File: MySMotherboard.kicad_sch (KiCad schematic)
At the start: 45 parts, among them IC1 TS5205, IC2 25SN, IC3 ATSHA204A, IC4 MCP1640CT-I/CHY, IC5 ATMEGA328P-AU, J1 SJ2W, J2 SJ, Q1 PMOSSOT23, Q2 FA-128, X1 JST-PH2, X2 MA10-2

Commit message: refactor schematic to use native KiCad symbols and footprints
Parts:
- removed ANT0: WIREPAD2,15/1,0, MySMotherboard:2,15_1,0, symbol MySMotherboard-eagle-import:WIREPAD2,15/1,0
- removed BTN0, RST0: DTSM-3, MySMotherboard:DTSM-3, symbol MySMotherboard-eagle-import:DTSM-3
- removed C1, C13, C14, C3: 10u, MySMotherboard:C0603K, symbol MySMotherboard-eagle-import:C-EUC0603K
- removed C10, C4, C5, C6, C7: 100n, MySMotherboard:C0402, symbol MySMotherboard-eagle-import:C-EUC0402
- removed C12: 10n, MySMotherboard:C0402, symbol MySMotherboard-eagle-import:C-EUC0402
- removed C2: 4.7u, MySMotherboard:C0603K, symbol MySMotherboard-eagle-import:C-EUC0603K
- removed C8, C9: 22p, MySMotherboard:0402-CAP, symbol MySMotherboard-eagle-import:CAP0402-CAP
- removed CR123A0: BAT_PACKCR123A, MySMotherboard:BH123A, symbol MySMotherboard-eagle-import:BAT_PACKCR123A
- removed CR2032: WA-BCPH_SMT_79527141, MySMotherboard:79527141, symbol MySMotherboard-eagle-import:WA-BCPH_SMT_79527141
- removed D1: LEDCHIP-LED0805, MySMotherboard:CHIP-LED0805, symbol MySMotherboard-eagle-import:LEDCHIP-LED0805
- removed IC1: TS5205, MySMotherboard:SOT25, symbol MySMotherboard-eagle-import:TS5205
- removed IC2: 25SN, MySMotherboard:SO-08, symbol MySMotherboard-eagle-import:25SN
- removed IC3: ATSHA204A, MySMotherboard:SOT23, symbol MySMotherboard-eagle-import:ATSHA204A
- removed IC4: MCP1640CT-I/CHY, MySMotherboard:SOT95P270X145-6N, symbol MySMotherboard-eagle-import:MCP1640CT-I/CHY
- removed IC5: ATMEGA328P-AU, MySMotherboard:QFP80P900X900X120-32N, symbol MySMotherboard-eagle-import:ATMEGA328P-AU
- removed J1: SJ2W, MySMotherboard:SJ_2, symbol MySMotherboard-eagle-import:SJ2W
- removed J2: SJ, MySMotherboard:SJ, symbol MySMotherboard-eagle-import:SJ
- removed L1: 4.7u, MySMotherboard:L3225P, symbol MySMotherboard-eagle-import:L-EUL3225P
- removed NRF24L01: WIRELESS-NRF24L01, MySMotherboard:WIRELESS-NRF24L01, symbol MySMotherboard-eagle-import:WIRELESS-NRF24L01
- removed Q1: PMOSSOT23, MySMotherboard:SOT-23, symbol MySMotherboard-eagle-import:PMOSSOT23
- removed Q2: FA-128, MySMotherboard:FA-128, symbol MySMotherboard-eagle-import:FA-128
- removed R1, R11, R2, R3, R7: 1M, MySMotherboard:R0603, symbol MySMotherboard-eagle-import:R-US_R0603
- removed R10, R9: 10k, MySMotherboard:R0603, symbol MySMotherboard-eagle-import:R-US_R0603
- removed R12: 0, MySMotherboard:0603-RES, symbol MySMotherboard-eagle-import:RESISTOR0603-RES
- removed R4: 620k, MySMotherboard:R0603, symbol MySMotherboard-eagle-import:R-US_R0603
- removed R5: 1M, MySMotherboard:0603-RES, symbol MySMotherboard-eagle-import:RESISTOR0603-RES
- removed R6: 100k, MySMotherboard:0603-RES, symbol MySMotherboard-eagle-import:RESISTOR0603-RES
- removed R8: 1k, MySMotherboard:R0603, symbol MySMotherboard-eagle-import:R-US_R0603
- removed RFM69W0: RFM69HW, MySMotherboard:RFM, symbol MySMotherboard-eagle-import:RFM69HW
- removed X1: JST-PH2, MySMotherboard:JST-PH2, symbol MySMotherboard-eagle-import:JST-PH2
- removed X2: MA10-2, MySMotherboard:MA10-2, symbol MySMotherboard-eagle-import:MA10-2
- added BT1: CR2032, Battery:BatteryHolder_Keystone_1060_1x2032, symbol Device:Battery_Cell
- added BT2: CR123A, MySMotherboard:BH123A, symbol Device:Battery_Cell
- added C1, C13, C2, C3: 10u, Capacitor_SMD:C_0603_1608Metric, symbol Device:C
- added C10, C12, C4, C5, C7: 100n, Capacitor_SMD:C_0402_1005Metric, symbol Device:C
- added C14: 10u/16V, Capacitor_SMD:C_0603_1608Metric, symbol Device:C
- added C8, C9: 22p, Capacitor_SMD:C_0402_1005Metric, symbol Device:C
- added D1: LED, LED_SMD:LED_0805_2012Metric_Pad1.15x1.40mm_HandSolder, symbol Device:LED
- added JP1, JP3: ~, Jumper:SolderJumper-2_P1.3mm_Open_RoundedPad1.0x1.5mm, symbol Jumper:Jumper_2_Open
- added JP2: ~, Jumper:SolderJumper-3_P1.3mm_Open_RoundedPad1.0x1.5mm, symbol Jumper:Jumper_3_Open
- added L1: 4.7u, Inductor_SMD:L_1210_3225Metric_Pad1.42x2.65mm_HandSolder, symbol Device:L
- added NRF24L1: WIRELESS-NRF24L01, MySMotherboard:WIRELESS-NRF24L01, symbol MySMotherboard:WIRELESS-NRF24L01
- added Q1: ~, Package_TO_SOT_SMD:SOT-23, symbol Device:Q_PMOS_GSD
- added R1, R11, R2, R3, R5, R7: 1M, Resistor_SMD:R_0603_1608Metric, symbol Device:R
- added R10, R9: 10k, Resistor_SMD:R_0603_1608Metric, symbol Device:R
- added R4: 620k, Resistor_SMD:R_0603_1608Metric, symbol Device:R
- added R6: 100k, Resistor_SMD:R_0603_1608Metric, symbol Device:R
- added R8: 1k, Resistor_SMD:R_0603_1608Metric, symbol Device:R
- added SW1: RST, Button_Switch_SMD:SW_SPST_EVQPE1, symbol Switch:SW_Push
- added SW2: BTN, Button_Switch_SMD:SW_SPST_EVQPE1, symbol Switch:SW_Push
- added U1: MCP1640Cx-xCHY, Package_TO_SOT_SMD:SOT-23-6, symbol Regulator_Switching:MCP1640Cx-xCHY
- added U2: APE8865Y5-30-HF-3, Package_TO_SOT_SMD:SOT-23-5, symbol Regulator_Linear:APE8865Y5-30-HF-3
- added U3: ATmega328PB-A, Package_QFP:TQFP-32_7x7mm_P0.8mm, symbol MCU_Microchip_ATmega:ATmega328PB-A
- added U4: AT25xxx, Package_SO:SOIC-8_3.9x4.9mm_P1.27mm, symbol Memory_EEPROM:AT25xxx
- added U5: RFM69HW, RF_Module:HOPERF_RFM69HW, symbol RF_Module:RFM69HW
- added U6: ATSHA204A, Package_TO_SOT_SMD:SOT-23, symbol MySMotherboard:ATSHA204A
- added X1: ~, Connector_JST:JST_PH_B2B-PH-K_1x02_P2.00mm_Vertical, symbol Connector:Conn_01x02_Pin
- added X2: MySX 2.5, Connector_PinHeader_2.54mm:PinHeader_2x10_P2.54mm_Vertical, symbol Connector_Generic:Conn_02x10_Odd_Even
- added X3: ANT, Connector_PinHeader_2.54mm:PinHeader_1x01_P2.54mm_Vertical, symbol Connector:Conn_01x01_Pin
- added Y1: 16M, Crystal:Crystal_SMD_2520-4Pin_2.5x2.0mm, symbol Device:Crystal_GND24
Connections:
- net A0: now also U3.23 (PC0), X2.8 (Pin_8)
- net A1: now also R8.2, U3.24 (PC1), X2.20 (Pin_20)
- net A2: now also R11.1, U1.3 (EN), U3.25 (PC2)
- net A3: now also U3.26 (PC3), U6.1 (SDA)
- net A4: now also R10.2, U3.27 (PC4), X2.14 (Pin_14)
- net A5: now also R9.2, U3.28 (PC5), X2.13 (Pin_13)
- net A7: now also C4.1, R5.2, R6.1, U3.22 (PE3)
- net D10: now also NRF24L1.4 (CSN), R1.2, U3.14 (PB2), U5.15 (NSS)
- net D2: now also JP3.1 (A), U3.32 (PD2), X2.9 (Pin_9)
- net D3: now also SW2.1, U3.1 (PD3), X2.10 (Pin_10)
- net D4: now also U3.2 (PD4), X2.15 (Pin_15)
- net D5: now also U3.9 (PD5), X2.11 (Pin_11)
- net D6: now also U3.10 (PD6), X2.12 (Pin_12)
- net D7: now also U3.11 (PD7), X2.16 (Pin_16)
- net D8: now also R2.2, U3.12 (PB0), U4.1 (~{CS})
- net D9: now also NRF24L1.3 (CE), U3.13 (PB1)
- net GND: now also BT1.2 (-), BT2.2 (-), C1.1, C10.2, C12.2, C13.2, C14.2, C2.2, C3.2, C4.2, C5.2, C7.2, C8.1, C9.2, NRF24L1.1 (GND), Q1.1 (G), R11.2, R4.2, R6.2, SW1.2, SW2.2, U1.2 (GND), U2.2 (GND), U3.21 (GND), U3.5 (GND), U4.4 (GND), U5.11 (GND), U5.9 (GND), U6.3 (GND), X1.2 (Pin_2), X2.4 (Pin_4), Y1.2, Y1.4
- net MISO: now also NRF24L1.7 (MISO), U3.16 (PB4), U4.2 (MISO), U5.13 (MISO), X2.18 (Pin_18)
- net MOSI: now also NRF24L1.6 (MOSI), U3.15 (PB3), U4.5 (MOSI), U5.14 (MOSI), X2.17 (Pin_17)
- net RST: now also R7.2, SW1.1, U3.29 (~{RESET}/PC6), X2.7 (Pin_7)
- net RX: now also U3.30 (PD0), X2.6 (Pin_6)
- net SCK: now also NRF24L1.5 (SCK), U3.17 (PB5), U4.6 (SCK), U5.12 (SCK), X2.19 (Pin_19)
- net TX: now also U3.31 (PD1), X2.5 (Pin_5)
- net VBAT: now also C14.1, C2.1, L1.1, Q1.2 (S), R5.1, U1.6 (V_{IN}), U2.1 (VIN), U2.3 (~{SHDN})
- net VBOOST: now also C3.1, JP2.1 (A), R3.1, U1.5 (V_{OUT})
- net VCC: now also C1.2, C5.1, C7.1, D1.2 (A), JP2.2 (C), NRF24L1.2 (VCC), R1.1, R10.1, R2.1, R7.1, R9.1, U3.18 (AVCC), U3.4 (VCC), U4.3 (~{WP}), U4.7 (~{HOLD}), U4.8 (VCC), U5.8 (3.3V), U6.2 (VCC), X2.2 (Pin_2), X2.3 (Pin_3)
- net VRAW: now also JP1.1 (A), X2.1 (Pin_1)
- net VREG: now also C13.1, JP2.3 (B), U2.5 (VOUT)
- new net: JP3.2 (B), NRF24L1.8 (IRQ), U5.2 (DIO0)
- new net: R3.2, R4.1, U1.4 (V_{FB})
- new net: D1.1 (K), R8.1
- new net: C12.1, U2.4 (BYP)
- new net: C8.2, U3.8 (XTAL2/PB7), Y1.1
- new net: C9.1, U3.7 (XTAL1/PB6), Y1.3
- new net: U5.10 (ANA), X3.1 (Pin_1)
- new net: C10.1, U3.20 (AREF)
- new net SW_L: L1.2, U1.1 (SW)
- new net VIN: BT1.1 (+), BT2.1 (+), JP1.2 (B), Q1.3 (D), X1.1 (Pin_1)
- no-connect marks 0 -> 9
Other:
- note added: "Crypto"
- note added: "DC/DC boost comverter"
- note added: "LDO Regulator"
- note added: "MCU"
- note added: "MySX Connector"
- note added: "Power supply selection"
- note added: "RF Modules"
- note added: "SPI EEPROM"
- company: (none) -> Marek Czerski
- title: (none) -> MYSMotherboard

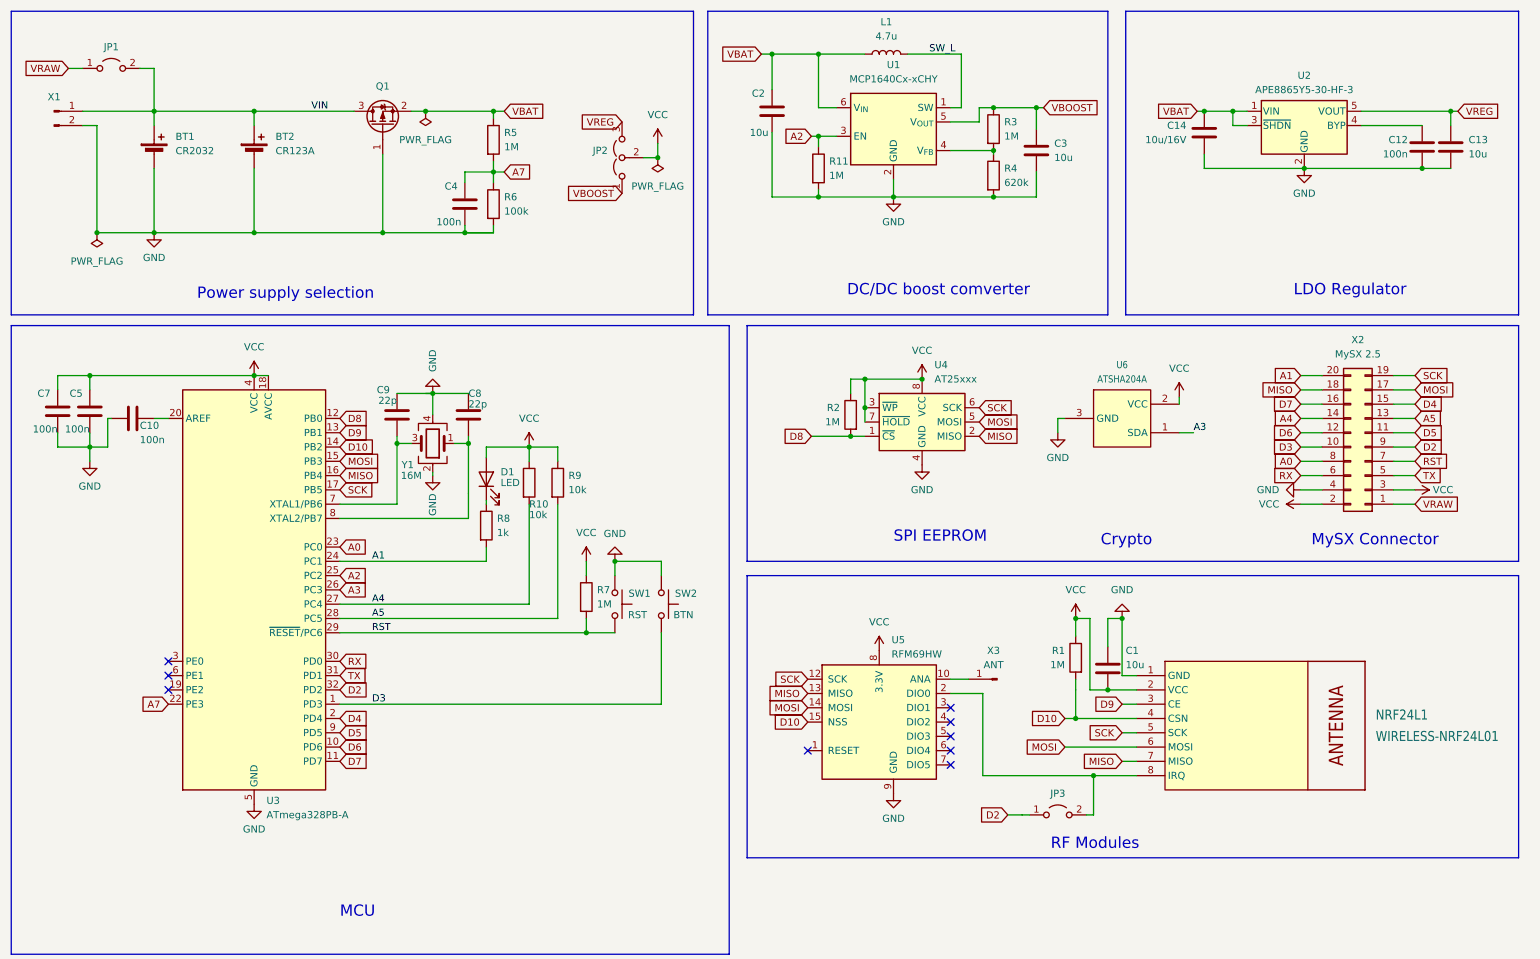
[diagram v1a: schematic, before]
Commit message: replace NRF24L01 with RS485 inteface
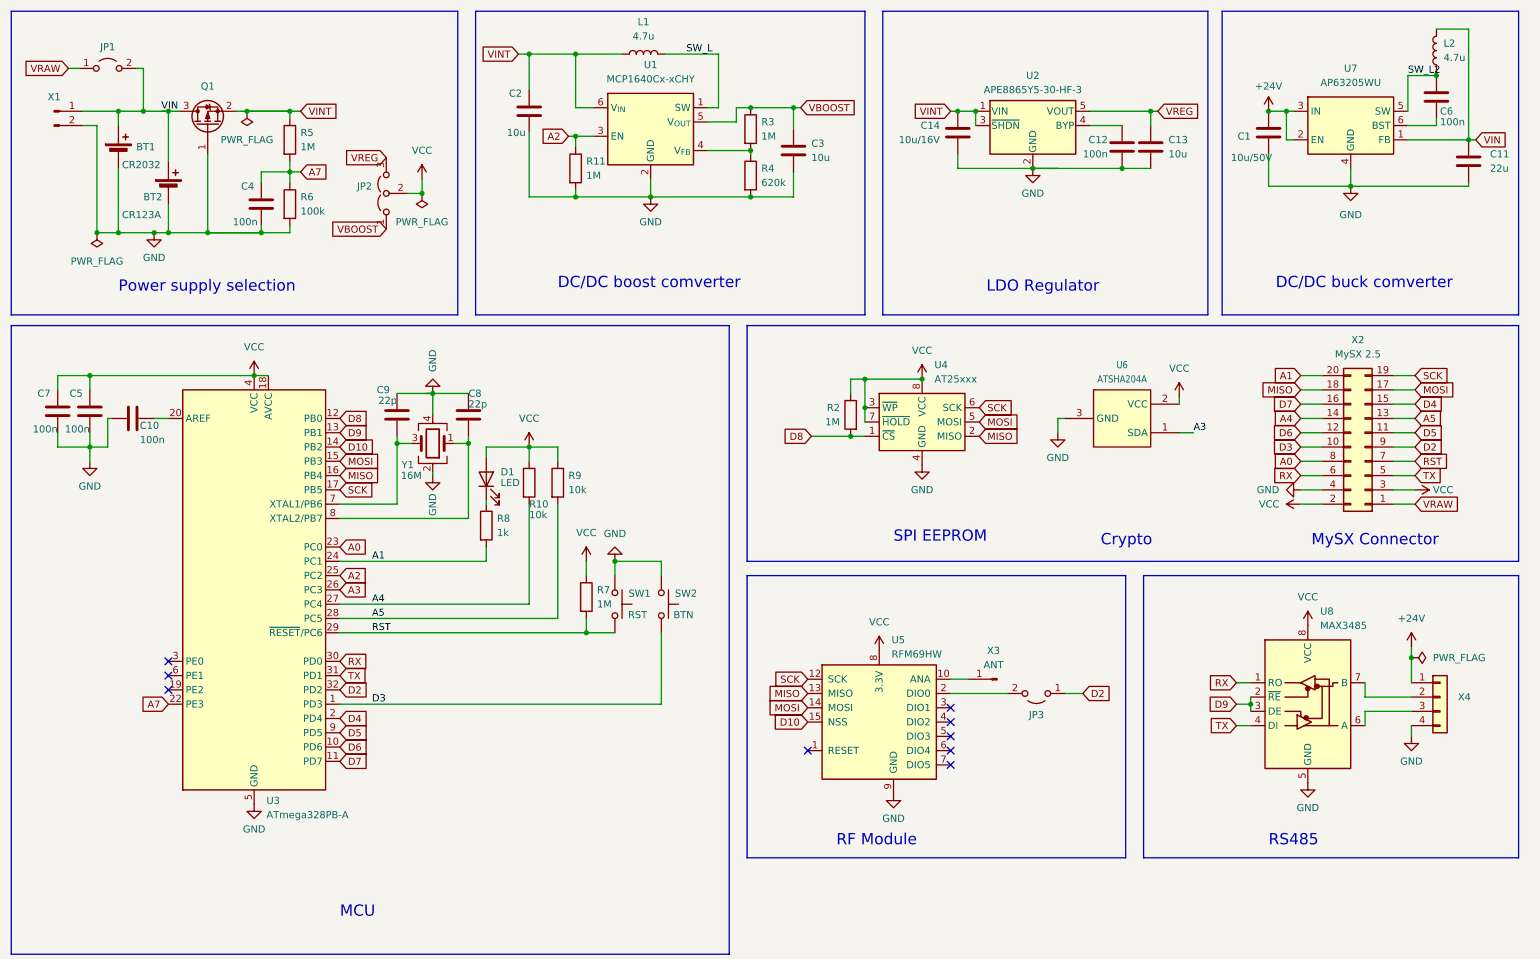
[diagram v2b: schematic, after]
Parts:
- removed NRF24L1: WIRELESS-NRF24L01, MySMotherboard:WIRELESS-NRF24L01, symbol MySMotherboard:WIRELESS-NRF24L01
- removed R1: 1M, Resistor_SMD:R_0603_1608Metric, symbol Device:R
- added C11: 22u, Capacitor_SMD:C_1206_3216Metric, symbol Device:C
- added C6: 100n, Capacitor_SMD:C_0402_1005Metric, symbol Device:C
- added L2: 4.7u, Inductor_SMD:L_1210_3225Metric, symbol Device:L
- added U7: AP63205WU, Package_TO_SOT_SMD:TSOT-23-6, symbol Regulator_Switching:AP63205WU
- added U8: MAX3485, Package_SO:SOIC-8_3.9x4.9mm_P1.27mm, symbol Interface_UART:MAX3485
- added X4: ~, TerminalBlock_Phoenix:TerminalBlock_Phoenix_MPT-0,5-4-2.54_1x04_P2.54mm_Horizontal, symbol Connector_Generic:Conn_01x04
- C1: value 10u -> 10u/50V; footprint Capacitor_SMD:C_0603_1608Metric -> Capacitor_SMD:C_1206_3216Metric
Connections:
- net D9: now also U8.2 (~{RE}), U8.3 (DE)
- net GND: now also C1.2, C11.2, U7.4 (GND), U8.5 (GND), X4.4 (Pin_4); no longer C1.1
- net RX: now also U8.1 (RO)
- net TX: now also U8.4 (DI)
- net VCC: now also U8.8 (VCC); no longer C1.2
- net VIN: now also C11.1, L2.2, U7.1 (FB)
- net VBAT renamed VINT
- new net: C6.1, U7.6 (BST)
- new net: U8.6 (A), X4.3 (Pin_3)
- new net: U8.7 (B), X4.2 (Pin_2)
- new net +24V: C1.1, U7.2 (EN), U7.3 (IN), X4.1 (Pin_1)
- new net SW_L2: C6.2, L2.1, U7.5 (SW)
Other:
- note added: "DC/DC buck comverter"
- note added: "RF Module"
- note added: "RS485"
- note removed: "RF Modules"
- moved on the sheet: BT1, BT2, C12, C13, C14, C2, C3, C4, JP1, JP2, JP3, L1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

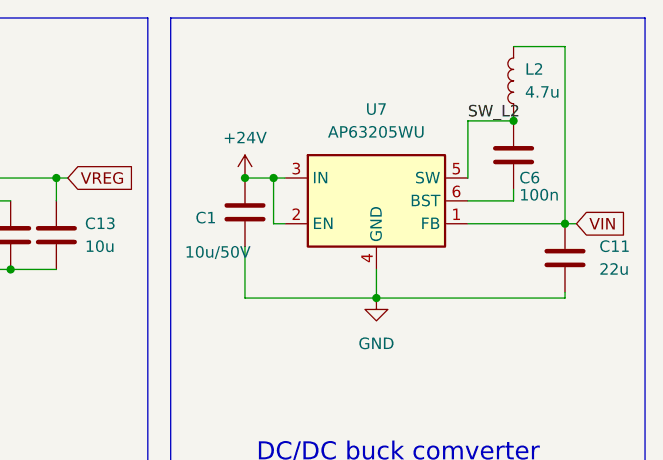
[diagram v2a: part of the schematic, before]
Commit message: change bypass capacitor for buck dc/dc converter to 50V 0603
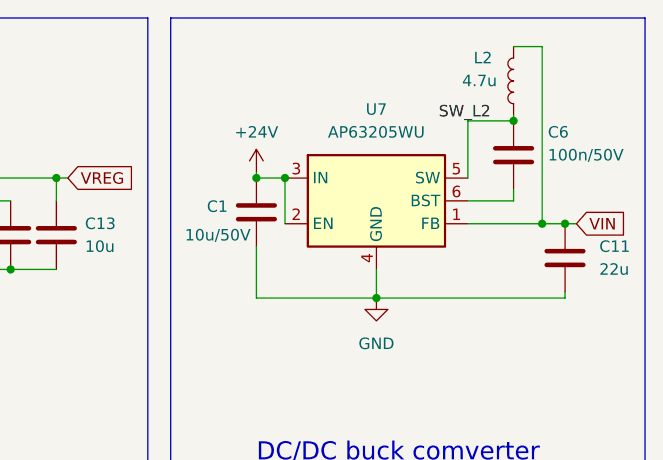
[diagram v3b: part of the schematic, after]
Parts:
- C6: value 100n -> 100n/50V; footprint Capacitor_SMD:C_0402_1005Metric -> Capacitor_SMD:C_0603_1608Metric_Pad1.08x0.95mm_HandSolder
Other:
- moved on the sheet: C1

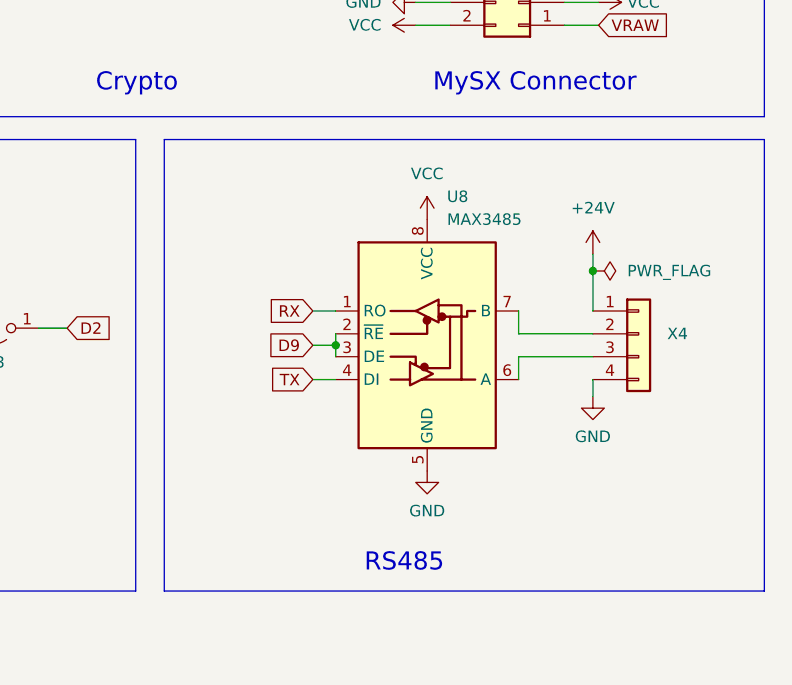
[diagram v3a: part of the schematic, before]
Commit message: add protection circuitry for RS485 IC AB lines
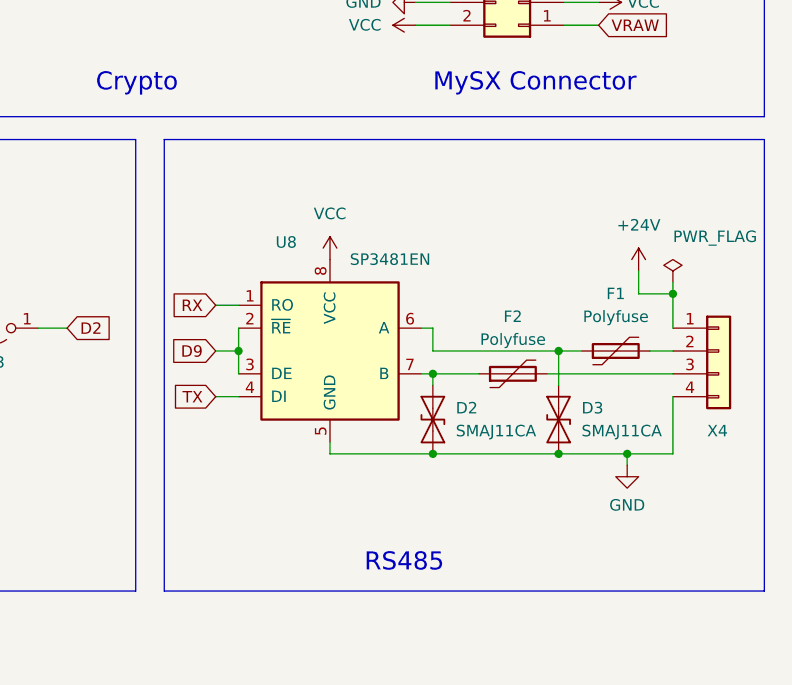
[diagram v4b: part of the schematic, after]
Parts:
- removed U8: MAX3485, Package_SO:SOIC-8_3.9x4.9mm_P1.27mm, symbol Interface_UART:MAX3485
- added D2, D3: SMAJ11CA, Diode_SMD:D_SMA, symbol Diode:SMAJ11CA
- added F1, F2: Polyfuse, Fuse:Fuse_1206_3216Metric_Pad1.42x1.75mm_HandSolder, symbol Device:Polyfuse
- added U8: SP3481EN, Package_SO:SOIC-8_3.9x4.9mm_P1.27mm, symbol Interface_UART:SP3481EN
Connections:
- net D9: now also U8.2 (~{RE}), U8.3 (DE)
- net GND: now also D2.1 (A1), D3.1 (A1), U8.5 (GND)
- net RX: now also U8.1 (RO)
- net TX: now also U8.4 (DI)
- net VCC: now also U8.8 (VCC)
- net at X4.3 (Pin_3): now also F2.2
- net at X4.2 (Pin_2): now also F1.2
- new net: D3.2 (A2), F1.1, U8.6 (A)
- new net: D2.2 (A2), F2.1, U8.7 (B)
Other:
- moved on the sheet: X4
